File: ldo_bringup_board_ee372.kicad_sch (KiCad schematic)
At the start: 73 parts, among them J1 VIN, J10 MD_SW_EN, J13 VSIG, J14 VSIG_BUF, J2 GND, J3 IBIAS, J4 VOUT, J5 VIN_SMA, J6 VOUT_SMA, J7 GND, J8 5V, Q1 FDV305N, Q2 FDV305N, Q3 FDV305N, Q4 FDV305N, Q5 FDV305N, SW1 SW_SPDT, U1 LDO_DualMode_BGR_EE372

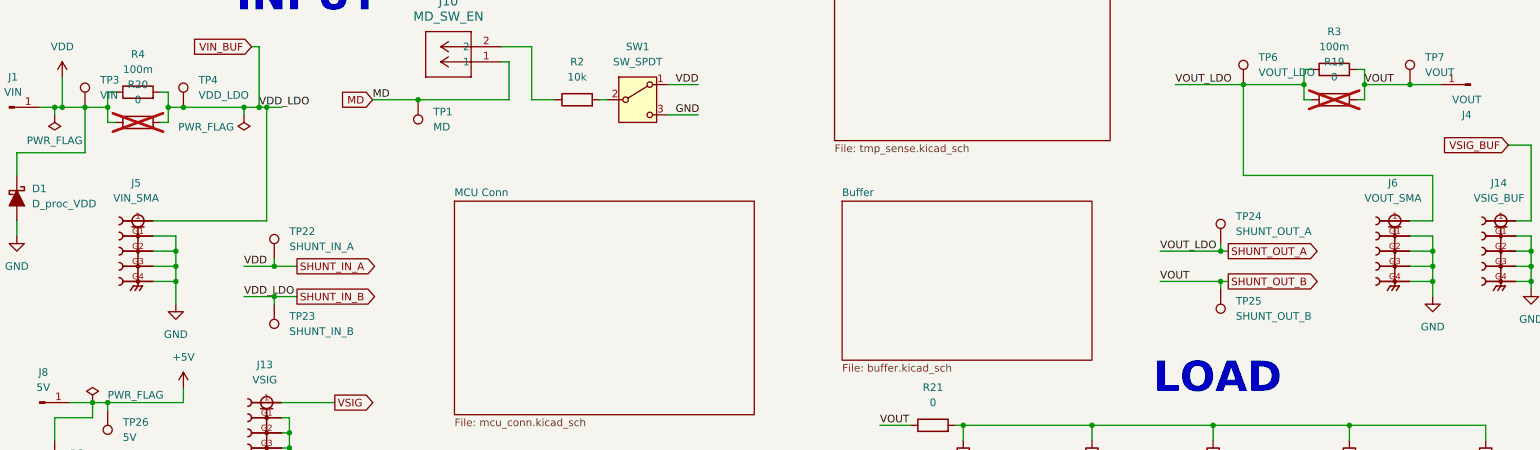
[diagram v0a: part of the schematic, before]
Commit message: Put the SMA coupling caps back on J5 and J6
C8 (10u) goes back between J5 and VDD_LDO (SHUNT_IN_B), and C10 (10u)
between J6 and VOUT_LDO (SHUNT_OUT_A), both the 1206 KEMET part. A 50 ohm
instrument on either SMA then sees only the ripple and draws no DC from the
chip, and J6 is the AC-coupled VOUT output the guidelines ask for.
Into 50 ohm the corner is 318 Hz.

118 parts, 86 nets, ERC 0 errors.
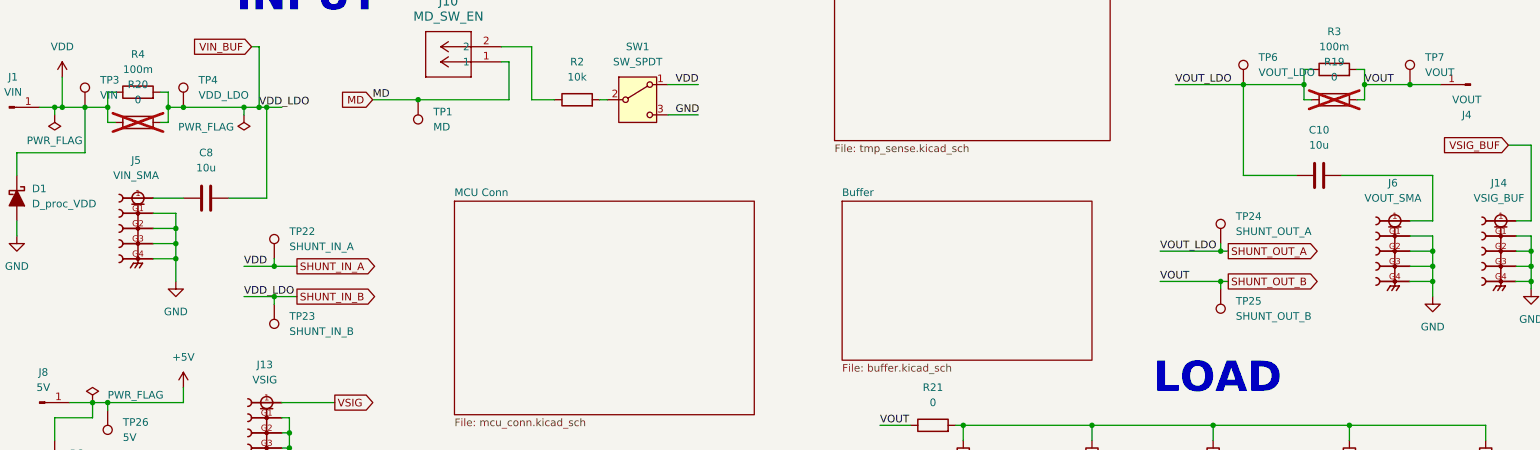
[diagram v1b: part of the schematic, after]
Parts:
- added C10, C8: 10u, Capacitor_SMD:C_1206_3216Metric_Pad1.33x1.80mm_HandSolder, symbol Device:C
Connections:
- net SHUNT_IN_B: now also C8.2; no longer J5.1
- net SHUNT_OUT_A: now also C10.1; no longer J6.1
- new net: C8.1, J5.1
- new net: C10.2, J6.1
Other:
- moved on the sheet: J5
